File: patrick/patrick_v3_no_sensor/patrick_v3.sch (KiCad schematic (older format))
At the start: 13 parts, among them J1 Conn_01x10, Q1 Q_NMOS_GSD, Q2 Q_NMOS_GSD, Q3 Q_NMOS_GSD, Q4 Q_NMOS_GSD

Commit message: switched connectors
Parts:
- removed J1: Conn_01x10, MolexPicoClasp:Molex_Pico-Clasp_501331-1007_1x10-1MP_P1.00mm_Vertical, symbol Connector_Generic:Conn_01x10
- added J1: Conn_02x05_Counter_Clockwise, Connector_PinSocket_2.00mm:PinSocket_2x05_P2.00mm_Vertical_SMD, symbol Connector_Generic:Conn_02x05_Counter_Clockwise
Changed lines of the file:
@@
 	3550 5300 5300 5300
-$Comp
-L Connector_Generic:Conn_01x10 J1
-U 1 1 6041AB42
-P 5500 2650
-F 0 "J1" H 5580 2642 50  0000 L CNN
-F 1 "Conn_01x10" H 5580 2551 50  0000 L CNN
-F 2 "MolexPicoClasp:Molex_Pico-Clasp_501331-1007_1x10-1MP_P1.00mm_Vertical" H 5500 2650 50  0001 C CNN
-F 3 "~" H 5500 2650 50  0001 C CNN
-	1    5500 2650
-	1    0    0    -1
-$EndComp
 $Comp
 L power:GND #PWR0101
@@
 Wire Wire Line
 	4100 3700 4300 3700
+$Comp
+L Connector_Generic:Conn_02x05_Counter_Clockwise J1
+U 1 1 60669BB9
+P 5700 2800
+F 0 "J1" H 5750 3217 50  0000 C CNN
+F 1 "Conn_02x05_Counter_Clockwise" H 5750 3126 50  0000 C CNN
+F 2 "Connector_PinSocket_2.00mm:PinSocket_2x05_P2.00mm_Vertical_SMD" H 5700 2800 50  0001 C CNN
+F 3 "~" H 5700 2800 50  0001 C CNN
+	1    5700 2800
+	1    0    0    -1
+$EndComp
 $EndSCHEMATC

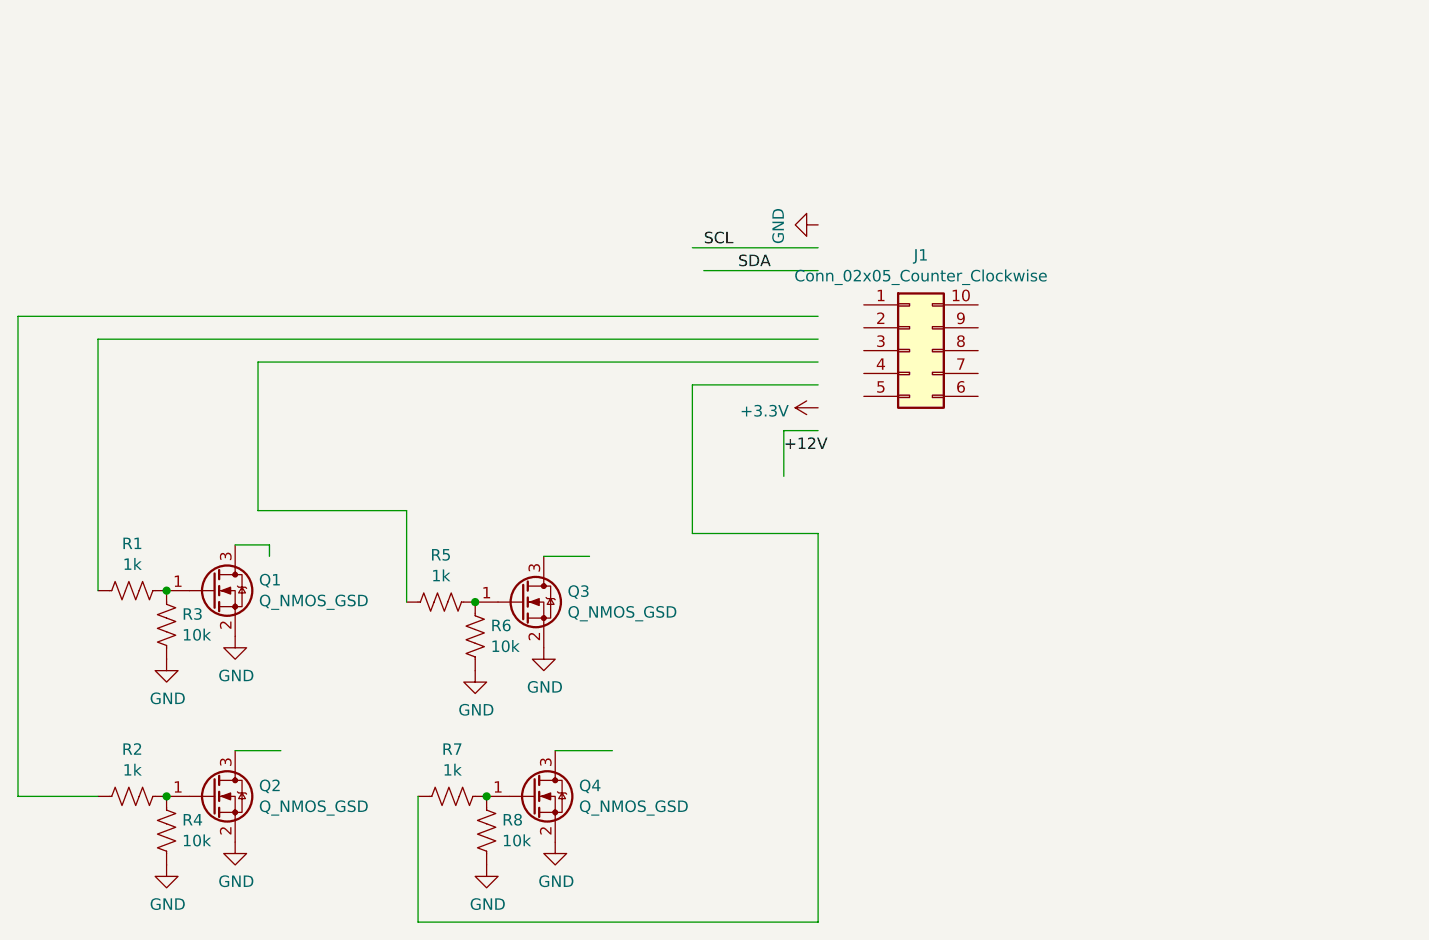
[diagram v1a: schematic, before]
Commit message: minigrid connectors instead of picoclasp
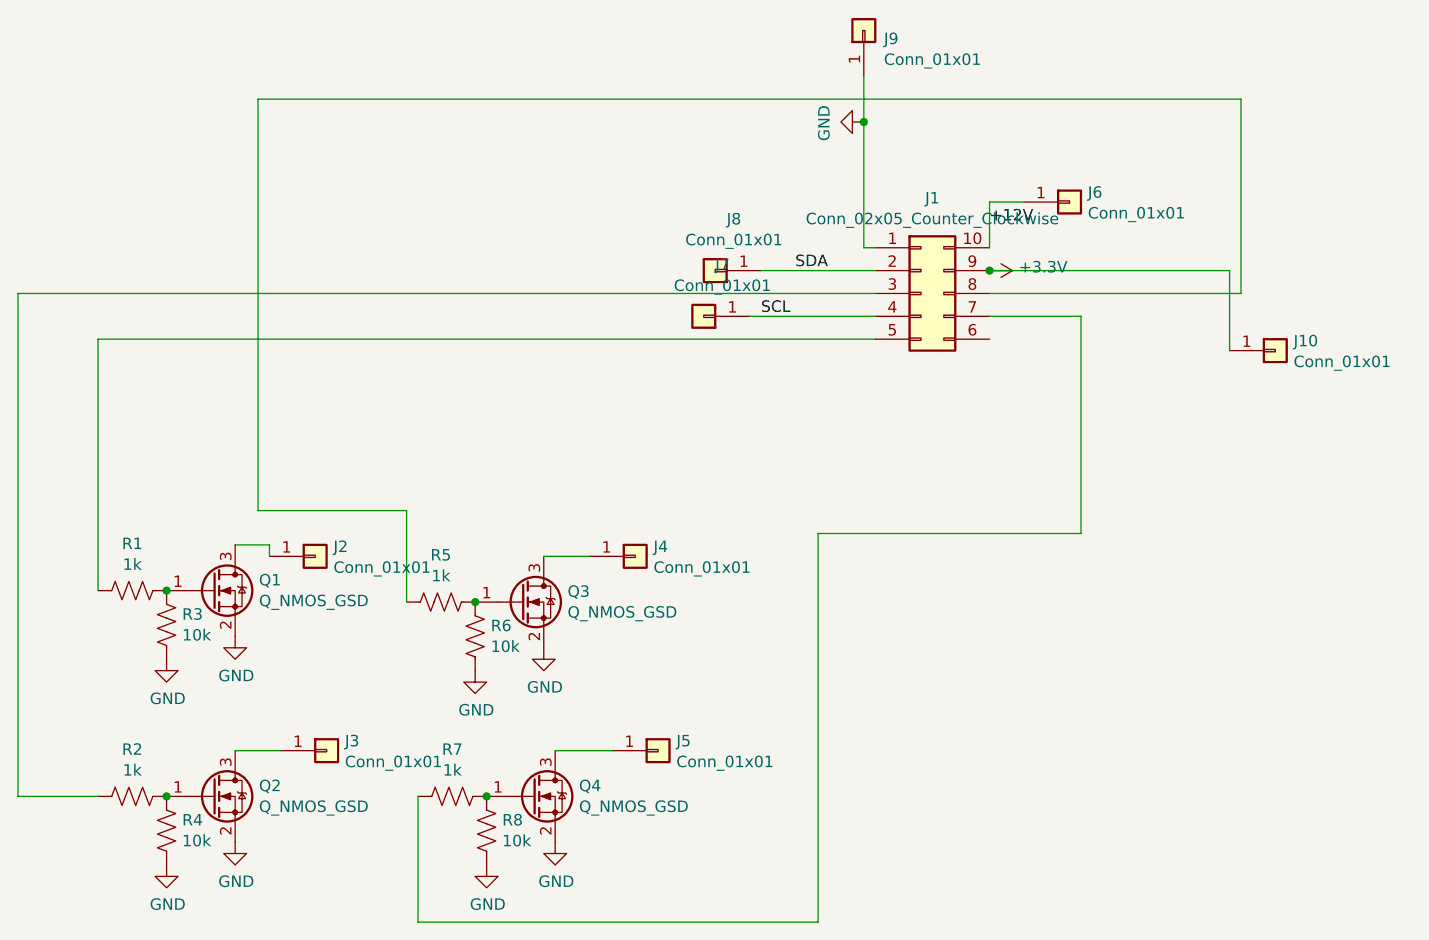
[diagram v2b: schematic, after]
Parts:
- added J10, J7, J8, J9: Conn_01x01, Connector_PinHeader_1.00mm:PinHeader_1x01_P1.00mm_Vertical, symbol Connector_Generic:Conn_01x01
- added J2, J3, J4, J5, J6: Conn_01x01, Connector_PinHeader_2.00mm:PinHeader_1x01_P2.00mm_Vertical, symbol Connector_Generic:Conn_01x01
- J1: footprint Connector_PinSocket_2.00mm:PinSocket_2x05_P2.00mm_Vertical_SMD -> molex_791091004:PinSocket_2x05_P2.00mm_Vertical_SMD
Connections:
- wire segments 24 -> 31
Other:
- moved on the sheet: J1
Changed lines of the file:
@@
 L power:+3.3V #PWR0109
 U 1 1 5FB6F8D6
-P 5300 3050
-F 0 "#PWR0109" H 5300 2900 50  0001 C CNN
-F 1 "+3.3V" V 5315 3178 50  0000 L CNN
-F 2 "" H 5300 3050 50  0001 C CNN
-F 3 "" H 5300 3050 50  0001 C CNN
-	1    5300 3050
-	0    -1   1    0
+P 6050 2450
+F 0 "#PWR0109" H 6050 2300 50  0001 C CNN
+F 1 "+3.3V" V 6065 2578 50  0000 L CNN
+F 2 "" H 6050 2450 50  0001 C CNN
+F 3 "" H 6050 2450 50  0001 C CNN
+	1    6050 2450
+	0    1    -1   0
 $EndComp
 Wire Wire Line
@@
 L power:GND #PWR0101
 U 1 1 6041E6F7
-P 5300 2250
-F 0 "#PWR0101" H 5300 2000 50  0001 C CNN
-F 1 "GND" H 5305 2077 50  0000 C CNN
-F 2 "" H 5300 2250 50  0001 C CNN
-F 3 "" H 5300 2250 50  0001 C CNN
-	1    5300 2250
+P 5500 1800
+F 0 "#PWR0101" H 5500 1550 50  0001 C CNN
+F 1 "GND" H 5505 1627 50  0000 C CNN
+F 2 "" H 5500 1800 50  0001 C CNN
+F 3 "" H 5500 1800 50  0001 C CNN
+	1    5500 1800
 	0    1    1    0
 $EndComp
 Wire Wire Line
-	5150 3350 5150 3150
-Wire Wire Line
-	5150 3150 5300 3150
-Text Label 5150 3250 0    50   ~ 0
+	6050 2350 6050 2150
+Wire Wire Line
+	6050 2150 6200 2150
+Text Label 6050 2250 0    50   ~ 0
 +12V
 Wire Wire Line
 	5300 5300 5300 3600
 Wire Wire Line
-	5300 3600 4750 3600
-Wire Wire Line
-	4750 3600 4750 2950
-Wire Wire Line
-	4750 2950 5300 2950
-Wire Wire Line
-	2850 3500 2850 2850
-Wire Wire Line
-	2850 2850 5300 2850
-Wire Wire Line
-	2150 2750 5300 2750
-Wire Wire Line
 	2150 2750 2150 3850
 Wire Wire Line
-	1800 2650 5300 2650
-Wire Wire Line
-	1800 2650 1800 4750
-Wire Wire Line
-	5300 2350 4750 2350
-Wire Wire Line
-	5300 2450 4800 2450
-Text Label 4800 2350 0    50   ~ 0
+	5550 2650 5000 2650
+Wire Wire Line
+	5550 2450 5050 2450
+Text Label 5050 2650 0    50   ~ 0
 SCL
-Text Label 4950 2450 0    50   ~ 0
+Text Label 5200 2450 0    50   ~ 0
 SDA
 Wire Wire Line
@@
 L Connector_Generic:Conn_02x05_Counter_Clockwise J1
 U 1 1 60669BB9
-P 5700 2800
-F 0 "J1" H 5750 3217 50  0000 C CNN
-F 1 "Conn_02x05_Counter_Clockwise" H 5750 3126 50  0000 C CNN
-F 2 "Connector_PinSocket_2.00mm:PinSocket_2x05_P2.00mm_Vertical_SMD" H 5700 2800 50  0001 C CNN
-F 3 "~" H 5700 2800 50  0001 C CNN
-	1    5700 2800
-	1    0    0    -1
-$EndComp
+P 5750 2550
+F 0 "J1" H 5800 2967 50  0000 C CNN
+F 1 "Conn_02x05_Counter_Clockwise" H 5800 2876 50  0000 C CNN
+F 2 "molex_791091004:PinSocket_2x05_P2.00mm_Vertical_SMD" H 5750 2550 50  0001 C CNN
+F 3 "~" H 5750 2550 50  0001 C CNN
+	1    5750 2550
+	1    0    0    -1
+$EndComp
+$Comp
+L Connector_Generic:Conn_01x01 J6
+U 1 1 60677AD6
+P 6400 2150
+F 0 "J6" H 6480 2192 50  0000 L CNN
+F 1 "Conn_01x01" H 6480 2101 50  0000 L CNN
+F 2 "Connector_PinHeader_2.00mm:PinHeader_1x01_P2.00mm_Vertical" H 6400 2150 50  0001 C CNN
+F 3 "~" H 6400 2150 50  0001 C CNN
+	1    6400 2150
+	1    0    0    -1
+$EndComp
+$Comp
+L Connector_Generic:Conn_01x01 J4
+U 1 1 60677ECD
+P 4500 3700
+F 0 "J4" H 4580 3742 50  0000 L CNN
+F 1 "Conn_01x01" H 4580 3651 50  0000 L CNN
+F 2 "Connector_PinHeader_2.00mm:PinHeader_1x01_P2.00mm_Vertical" H 4500 3700 50  0001 C CNN
+F 3 "~" H 4500 3700 50  0001 C CNN
+	1    4500 3700
+	1    0    0    -1
+$EndComp
+$Comp
+L Connector_Generic:Conn_01x01 J5
+U 1 1 60678DD4
+P 4600 4550
+F 0 "J5" H 4680 4592 50  0000 L CNN
+F 1 "Conn_01x01" H 4680 4501 50  0000 L CNN
+F 2 "Connector_PinHeader_2.00mm:PinHeader_1x01_P2.00mm_Vertical" H 4600 4550 50  0001 C CNN
+F 3 "~" H 4600 4550 50  0001 C CNN
+	1    4600 4550
+	1    0    0    -1
+$EndComp
+$Comp
+L Connector_Generic:Conn_01x01 J3
+U 1 1 606791C9
+P 3150 4550
+F 0 "J3" H 3230 4592 50  0000 L CNN
+F 1 "Conn_01x01" H 3230 4501 50  0000 L CNN
+F 2 "Connector_PinHeader_2.00mm:PinHeader_1x01_P2.00mm_Vertical" H 3150 4550 50  0001 C CNN
+F 3 "~" H 3150 4550 50  0001 C CNN
+	1    3150 4550
+	1    0    0    -1
+$EndComp
+$Comp
+L Connector_Generic:Conn_01x01 J2
+U 1 1 6067975F
+P 3100 3700
+F 0 "J2" H 3180 3742 50  0000 L CNN
+F 1 "Conn_01x01" H 3180 3651 50  0000 L CNN
+F 2 "Connector_PinHeader_2.00mm:PinHeader_1x01_P2.00mm_Vertical" H 3100 3700 50  0001 C CNN
+F 3 "~" H 3100 3700 50  0001 C CNN
+	1    3100 3700
+	1    0    0    -1
+$EndComp
+Wire Wire Line
+	2850 1700 7150 1700
+Wire Wire Line
+	7150 1700 7150 2550
+Wire Wire Line
+	7150 2550 6050 2550
+Wire Wire Line
+	2850 1700 2850 3500
+Wire Wire Line
+	1800 2550 5550 2550
+Wire Wire Line
+	1800 2550 1800 4750
+Wire Wire Line
+	2150 2750 5550 2750
+Wire Wire Line
+	5300 3600 6450 3600
+Wire Wire Line
+	6450 3600 6450 2650
+Wire Wire Line
+	6450 2650 6050 2650
+$Comp
+L Connector_Generic:Conn_01x01 J10
+U 1 1 606A2E97
+P 7300 2800
+F 0 "J10" H 7380 2842 50  0000 L CNN
+F 1 "Conn_01x01" H 7380 2751 50  0000 L CNN
+F 2 "Connector_PinHeader_1.00mm:PinHeader_1x01_P1.00mm_Vertical" H 7300 2800 50  0001 C CNN
+F 3 "~" H 7300 2800 50  0001 C CNN
+	1    7300 2800
+	1    0    0    -1
+$EndComp
+$Comp
+L Connector_Generic:Conn_01x01 J8
+U 1 1 606A3297
+P 4850 2450
+F 0 "J8" H 4768 2225 50  0000 C CNN
+F 1 "Conn_01x01" H 4768 2316 50  0000 C CNN
+F 2 "Connector_PinHeader_1.00mm:PinHeader_1x01_P1.00mm_Vertical" H 4850 2450 50  0001 C CNN
+F 3 "~" H 4850 2450 50  0001 C CNN
+	1    4850 2450
+	-1   0    0    1
+$EndComp
+$Comp
+L Connector_Generic:Conn_01x01 J7
+U 1 1 606A3657
+P 4800 2650
+F 0 "J7" H 4718 2425 50  0000 C CNN
+F 1 "Conn_01x01" H 4718 2516 50  0000 C CNN
+F 2 "Connector_PinHeader_1.00mm:PinHeader_1x01_P1.00mm_Vertical" H 4800 2650 50  0001 C CNN
+F 3 "~" H 4800 2650 50  0001 C CNN
+	1    4800 2650
+	-1   0    0    1
+$EndComp
+$Comp
+L Connector_Generic:Conn_01x01 J9
+U 1 1 606A39C0
+P 5500 1400
+F 0 "J9" V 5464 1312 50  0000 R CNN
+F 1 "Conn_01x01" V 5373 1312 50  0000 R CNN
+F 2 "Connector_PinHeader_1.00mm:PinHeader_1x01_P1.00mm_Vertical" H 5500 1400 50  0001 C CNN
+F 3 "~" H 5500 1400 50  0001 C CNN
+	1    5500 1400
+	0    -1   -1   0
+$EndComp
+Wire Wire Line
+	6050 2450 7100 2450
+Wire Wire Line
+	7100 2450 7100 2800
+Connection ~ 6050 2450
+Wire Wire Line
+	5500 1600 5500 1800
+Wire Wire Line
+	5500 2350 5550 2350
+Connection ~ 5500 1800
+Wire Wire Line
+	5500 1800 5500 2350
 $EndSCHEMATC

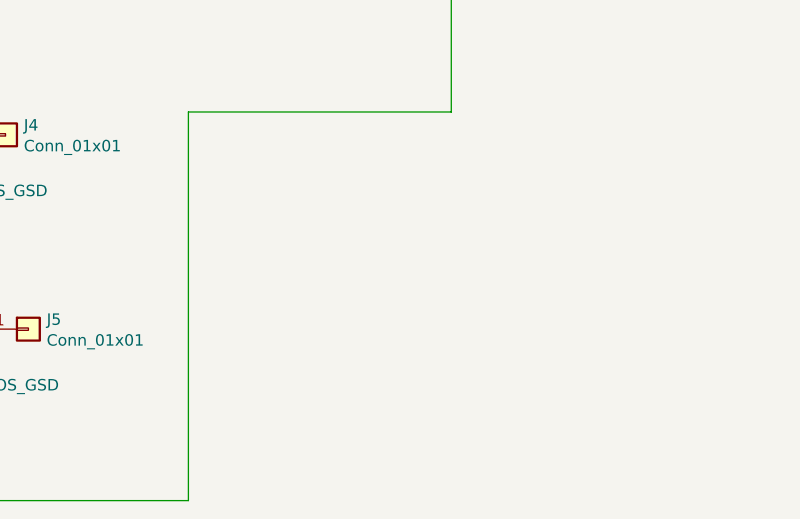
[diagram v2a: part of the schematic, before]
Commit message: added patrick board with bigger vias for battery wires
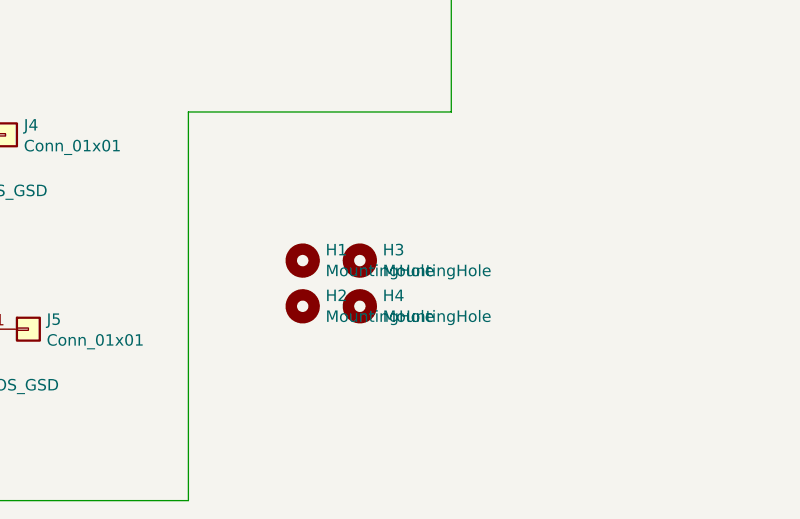
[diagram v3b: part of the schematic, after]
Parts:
- added H1, H2, H3, H4: MountingHole, MountingHole:MountingHole_2mm, symbol Mechanical:MountingHole
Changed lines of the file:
@@
 Wire Wire Line
 	5500 1800 5500 2350
+$Comp
+L Mechanical:MountingHole H1
+U 1 1 60675DAA
+P 5800 4250
+F 0 "H1" H 5900 4296 50  0000 L CNN
+F 1 "MountingHole" H 5900 4205 50  0000 L CNN
+F 2 "MountingHole:MountingHole_2mm" H 5800 4250 50  0001 C CNN
+F 3 "~" H 5800 4250 50  0001 C CNN
+	1    5800 4250
+	1    0    0    -1
+$EndComp
+$Comp
+L Mechanical:MountingHole H3
+U 1 1 6067608C
+P 6050 4250
+F 0 "H3" H 6150 4296 50  0000 L CNN
+F 1 "MountingHole" H 6150 4205 50  0000 L CNN
+F 2 "MountingHole:MountingHole_2mm" H 6050 4250 50  0001 C CNN
+F 3 "~" H 6050 4250 50  0001 C CNN
+	1    6050 4250
+	1    0    0    -1
+$EndComp
+$Comp
+L Mechanical:MountingHole H2
+U 1 1 6067667B
+P 5800 4450
+F 0 "H2" H 5900 4496 50  0000 L CNN
+F 1 "MountingHole" H 5900 4405 50  0000 L CNN
+F 2 "MountingHole:MountingHole_2mm" H 5800 4450 50  0001 C CNN
+F 3 "~" H 5800 4450 50  0001 C CNN
+	1    5800 4450
+	1    0    0    -1
+$EndComp
+$Comp
+L Mechanical:MountingHole H4
+U 1 1 60676DD5
+P 6050 4450
+F 0 "H4" H 6150 4496 50  0000 L CNN
+F 1 "MountingHole" H 6150 4405 50  0000 L CNN
+F 2 "MountingHole:MountingHole_2mm" H 6050 4450 50  0001 C CNN
+F 3 "~" H 6050 4450 50  0001 C CNN
+	1    6050 4450
+	1    0    0    -1
+$EndComp
 $EndSCHEMATC
